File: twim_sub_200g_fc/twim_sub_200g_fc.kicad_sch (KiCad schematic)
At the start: 40 parts, among them J1 GNSS_1, J2 GNSS_2, J3 ELRS, J4 BATTERY CONNECTOR, J5 SWD CONN, J7 VTX_CONN, J8 USB_CONN, M1 Motor_Servo, M2 Motor_Servo, M3 Motor_Servo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

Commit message: qsss
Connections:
- net PWM_3: no longer U1.2 (PC13)
- net PWM_4: now also U1.2 (PC13)
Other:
- moved on the sheet: C15, C5, C7, C8, H1, H2, J4, J7, Q1, R3, R4, R5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

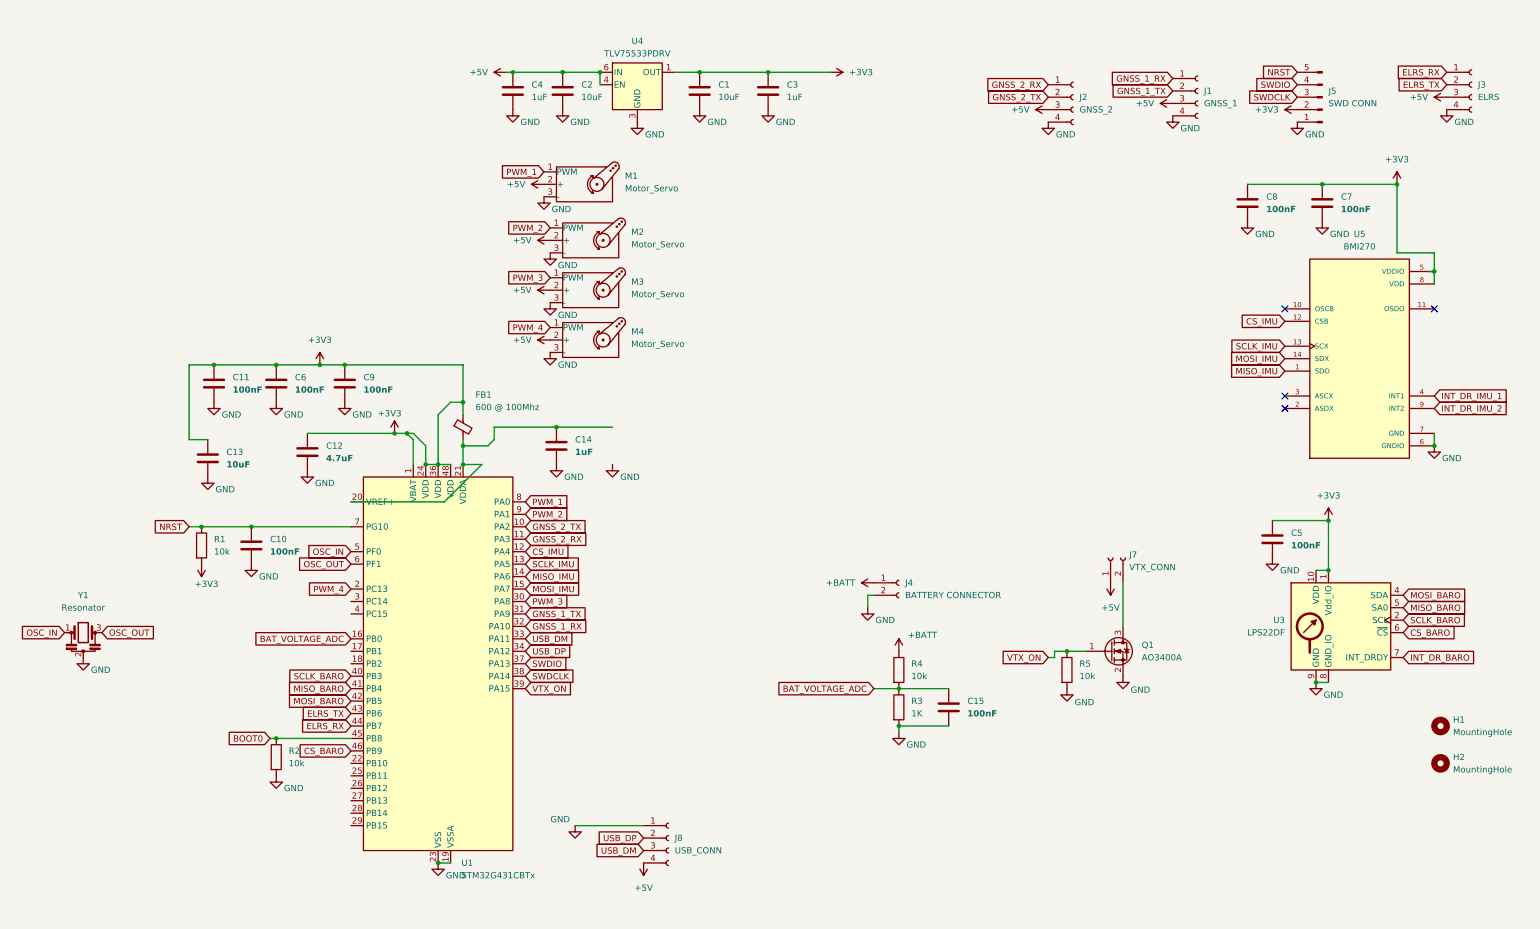
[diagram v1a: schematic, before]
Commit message: added main layout 22mmx30mm
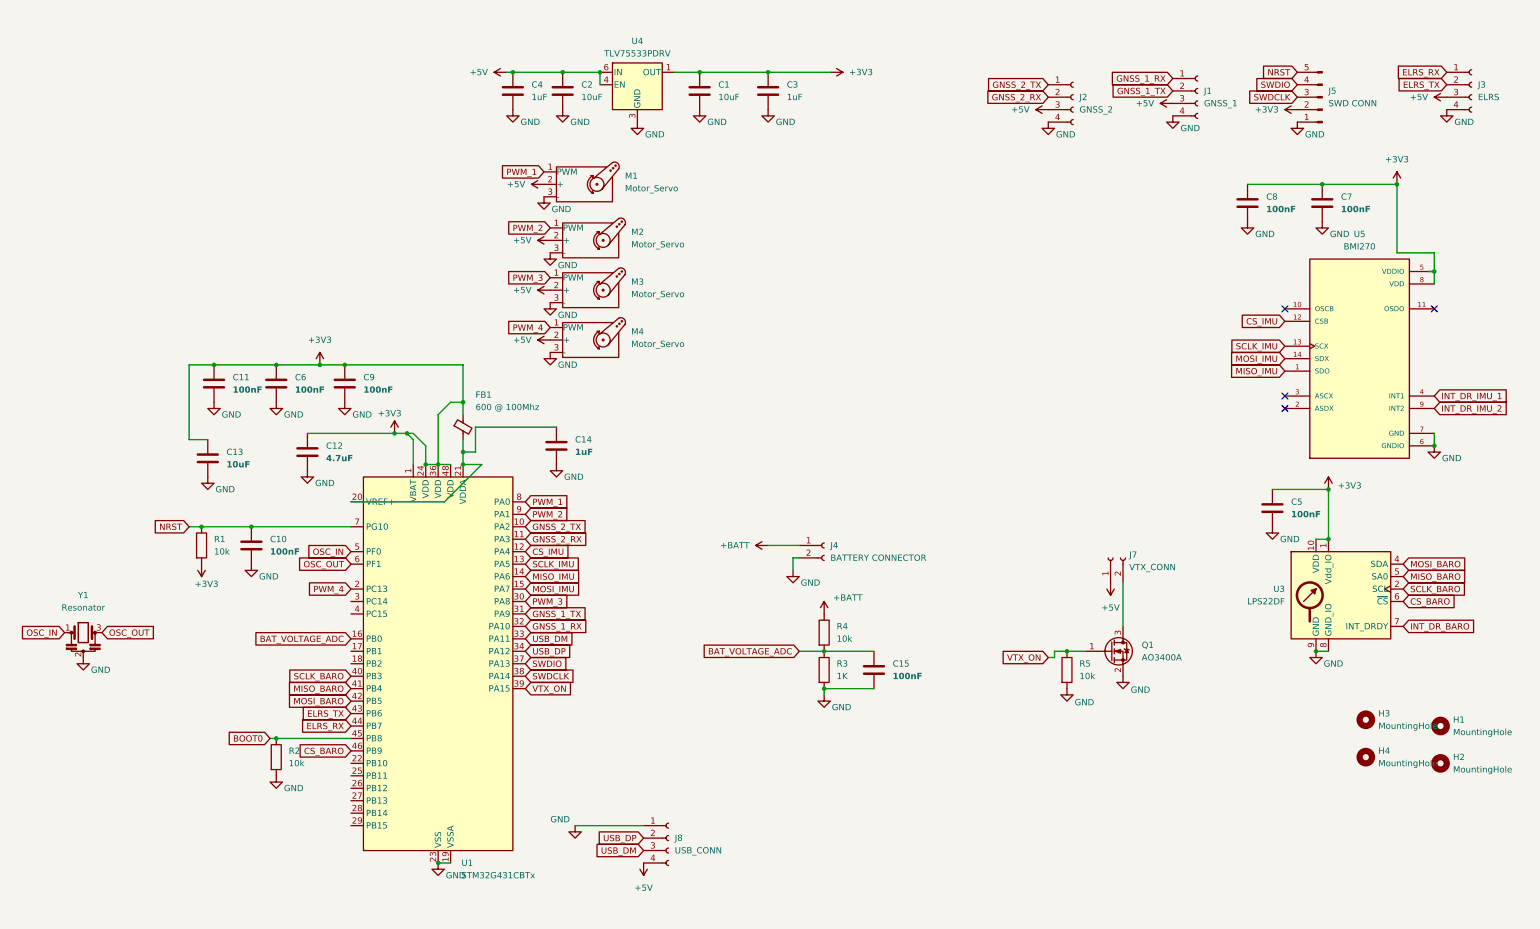
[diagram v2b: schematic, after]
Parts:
- added H3, H4: MountingHole, MountingHole:MountingHole_2.2mm_M2, symbol Mechanical:MountingHole
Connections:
- net GNSS_2_RX: now also J2.2 (Pin_2); no longer J2.1 (Pin_1)
- net GNSS_2_TX: now also J2.1 (Pin_1); no longer J2.2 (Pin_2)
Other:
- moved on the sheet: C15, C5, J4, R3, R4, U3

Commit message: added baselayout
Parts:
- removed J1: GNSS_1, smd_pads:01x04_smd_pad_1.2mm, symbol Connector:Conn_01x04_Socket
- removed M4: Motor_Servo, Connector_PinHeader_2.54mm:PinHeader_1x03_P2.54mm_Vertical, symbol Motor:Motor_Servo
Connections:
- net GNSS_1_RX is gone; now on net GNSS_2_RX: U1.32 (PA10)
- net GNSS_1_TX is gone; now on net GNSS_2_TX: U1.31 (PA9)
- net GNSS_2_RX: no longer U1.11 (PA3)
- net GNSS_2_TX: no longer U1.10 (PA2)
- net PWM_1: now also U1.9 (PA1); no longer U1.8 (PA0)
- net PWM_2: now also U1.8 (PA0); no longer U1.9 (PA1)
- net PWM_4: no longer names the net of U1.2 (PC13)
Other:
- moved on the sheet: J2

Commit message: adddd
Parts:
- removed Q1: AO3400A, Package_TO_SOT_SMD:SOT-23, symbol Transistor_FET:AO3400A
- removed U4: TLV75533PDRV, Package_SON:WSON-6-1EP_2x2mm_P0.65mm_EP1x1.6mm, symbol Regulator_Linear:TLV75533PDRV
- added Q2: DMG1012T, Package_TO_SOT_SMD:SOT-523, symbol Transistor_FET:DMG1012T
- added U2: AP2112K-3.3, PCM_SparkFun-Semiconductor-Standard:SOT23-5, symbol PCM_SparkFun-Regulator:AP2112K-3.3
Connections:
- net +3V3: now also U2.5 (VOUT)
- net +5V: now also J3.4 (Pin_4), U2.1 (VIN), U2.3 (EN); no longer J3.3 (Pin_3)
- net GND: now also J3.3 (Pin_3), Q2.2 (S), U2.2 (GND); no longer J3.4 (Pin_4)
- net GNSS_2_RX: now also J2.1 (Pin_1); no longer J2.2 (Pin_2)
- net GNSS_2_TX: now also J2.2 (Pin_2); no longer J2.1 (Pin_1)
- net INT_DR_BARO: now also U1.2 (PC13)
- net INT_DR_IMU_1: now also U1.17 (PB1)
- net INT_DR_IMU_2: now also U1.18 (PB2)
- net VTX_ON: now also U1.25 (PB11), Q2.1 (G); no longer U1.39 (PA15)
- net at J7.2 (Pin_2): now also Q2.3 (D)

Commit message: added tom's changes
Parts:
- removed J8: USB_CONN, Connector_JST:JST_SH_SM04B-SRSS-TB_1x04-1MP_P1.00mm_Horizontal, symbol Connector:Conn_01x04_Socket
- added C16: 1uF, Capacitor_SMD:C_0402_1005Metric, symbol Device:C
- added C21: 100nF, Capacitor_SMD:C_0402_1005Metric, symbol Device:C
- added J1: Conn_JST_SH_01x04_Horizontal_SMD, PCM_fab:Conn_JST_SH_01x04_Horizontal_SMD, symbol PCM_fab:Conn_JST_SH_01x04_Horizontal_SMD
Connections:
- net +5V: now also J2.4 (Pin_4), C16.1, C21.1, J1.4; no longer J2.3 (Pin_3)
- net GND: now also J2.3 (Pin_3), C16.2, C21.2, J1.1; no longer J2.4 (Pin_4)
- net USB_DM: now also J1.3
- net USB_DP: now also J1.2
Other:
- moved on the sheet: C10, C11, C12, C13, C14, C15, C6, C9, FB1, J4, J7, Q2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

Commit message: finished V1
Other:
- moved on the sheet: J1, J7, Q2, R5, Y1
